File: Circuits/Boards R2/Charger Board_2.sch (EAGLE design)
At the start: 78 parts, among them CON1 ISP(2X3), CON10 HEADER_3X1, CON11 HEADER_3X1, CON12 HEADER_3X1, CON13 HEADER_4X1, CON2 SCREWTERMINAL_1X2, CON3 HEADER_3X1, CON4 HEADER_3X1, CON5 HEADER_3X1, CON6 HEADER_3X1, CON7 HEADER_3X1, CON8 HEADER_3X1, CON9 HEADER_3X1, IC1 NCP1117DT33G, T1 NPN2N2222, T2 NPN2N2222, T3 SI4421DY, U1 ATMEGA324P, U2 ACS711, U3 JOYSTICKPTH, U4 MX25L25735E

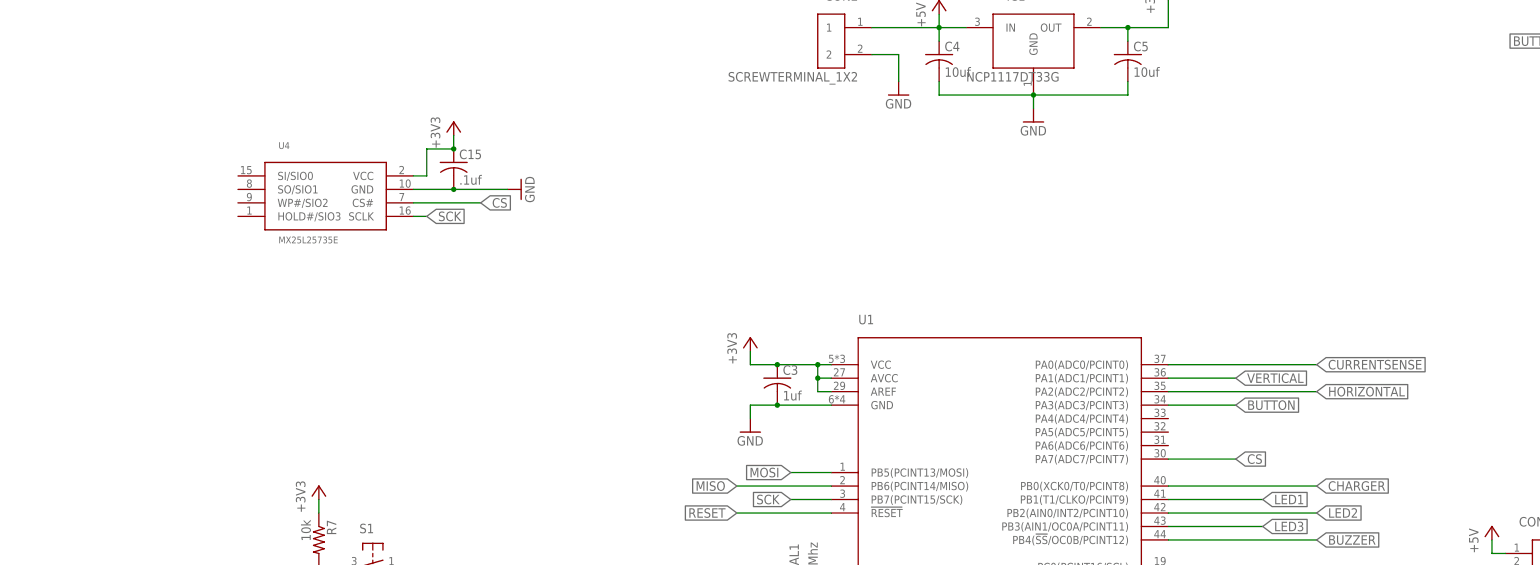
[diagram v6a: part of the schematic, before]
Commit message: completed schematic for the charger board
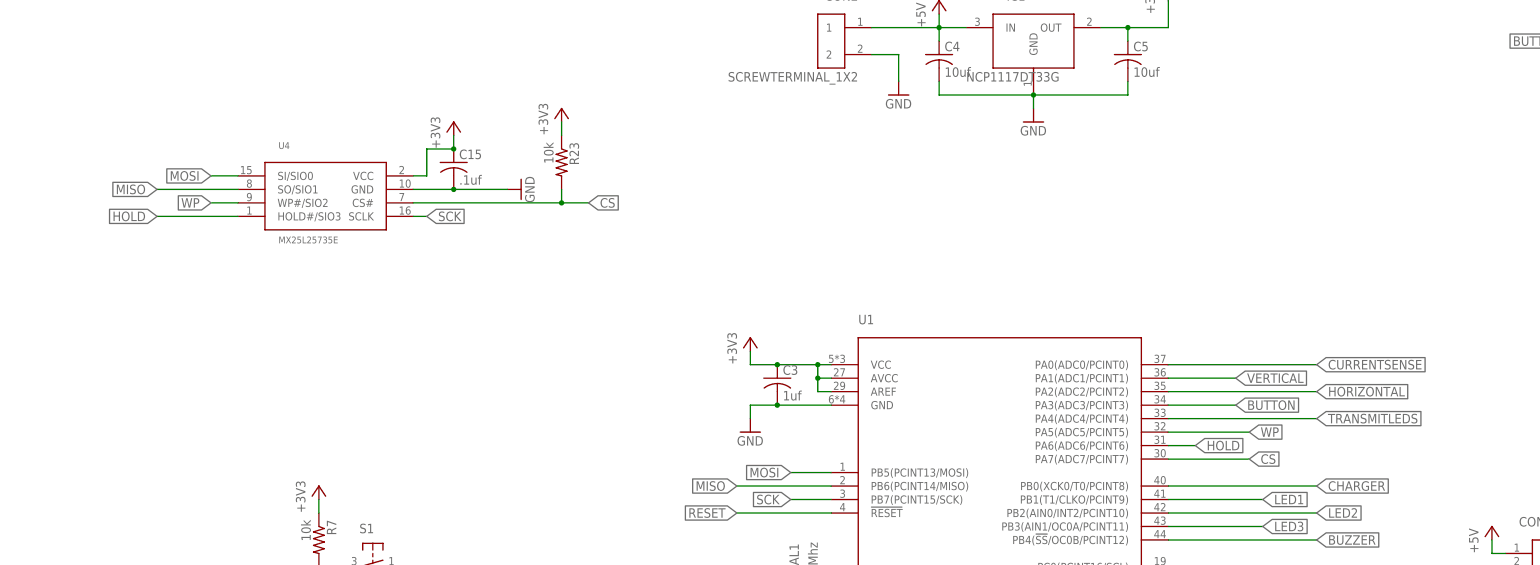
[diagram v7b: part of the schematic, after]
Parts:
- added R23: 10k, Passive:RES0603
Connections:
- new net HOLD: U1.PA6(ADC6/PCINT6), U4.HOLD#/SIO3
- new net WP: U1.PA5(ADC5/PCINT5), U4.WP#/SIO2
- net +3V3: now also R23.1
- net CS: now also R23.2
- net MISO: now also U4.SO/SIO1
- net MOSI: now also U4.SI/SIO0
- net TRANSMITLEDS: now also U1.PA4(ADC4/PCINT4)
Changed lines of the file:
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@@
 <part name="+3V1" library="Supply" deviceset="+3V3" device=""/>
 <part name="GND17" library="Supply" deviceset="GND" device=""/>
+<part name="R23" library="Passive" deviceset="RES" device="0603" value="10k"/>
+<part name="+3V11" library="Supply" deviceset="+3V3" device=""/>
 </parts>
 <sheets>
@@
 <instance part="+3V1" gate="G$1" x="-104.14" y="83.82"/>
 <instance part="GND17" gate="1" x="-91.44" y="71.12" rot="R90"/>
+<instance part="R23" gate="G$1" x="-83.82" y="76.2" rot="R270"/>
+<instance part="+3V11" gate="G$1" x="-83.82" y="86.36"/>
 </instances>
 <busses>
@@
 <wire x1="190.5" y1="43.18" x2="185.42" y2="43.18" width="0.1524" layer="91"/>
 <label x="185.42" y="43.18" size="1.778" layer="91" rot="R180" xref="yes"/>
+</segment>
+<segment>
+<pinref part="U1" gate="G$1" pin="PA4(ADC4/PCINT4)"/>
+<wire x1="30.48" y1="27.94" x2="58.42" y2="27.94" width="0.1524" layer="91"/>
+<label x="58.42" y="27.94" size="1.778" layer="91" xref="yes"/>
 </segment>
 </net>
@@
 <junction x="-104.14" y="78.74"/>
 </segment>
+<segment>
+<pinref part="R23" gate="G$1" pin="1"/>
+<wire x1="-83.82" y1="81.28" x2="-83.82" y2="83.82" width="0.1524" layer="91"/>
+<pinref part="+3V11" gate="G$1" pin="+3V3"/>
+</segment>
 </net>
 <net name="SECTION2" class="0">
@@
 <label x="-40.64" y="17.78" size="1.778" layer="91" rot="R180" xref="yes"/>
 </segment>
+<segment>
+<pinref part="U4" gate="G$1" pin="SI/SIO0"/>
+<wire x1="-144.78" y1="73.66" x2="-149.86" y2="73.66" width="0.1524" layer="91"/>
+<label x="-149.86" y="73.66" size="1.778" layer="91" rot="R180" xref="yes"/>
+</segment>
 </net>
 <net name="MISO" class="0">
@@
 <label x="-50.8" y="15.24" size="1.778" layer="91" rot="R180" xref="yes"/>
 </segment>
+<segment>
+<pinref part="U4" gate="G$1" pin="SO/SIO1"/>
+<wire x1="-144.78" y1="71.12" x2="-160.02" y2="71.12" width="0.1524" layer="91"/>
+<label x="-160.02" y="71.12" size="1.778" layer="91" rot="R180" xref="yes"/>
+</segment>
 </net>
 <net name="SCK" class="0">
@@
 <segment>
 <pinref part="U4" gate="G$1" pin="CS#"/>
-<wire x1="-111.76" y1="68.58" x2="-99.06" y2="68.58" width="0.1524" layer="91"/>
-<label x="-99.06" y="68.58" size="1.778" layer="91" xref="yes"/>
+<wire x1="-111.76" y1="68.58" x2="-83.82" y2="68.58" width="0.1524" layer="91"/>
+<label x="-78.74" y="68.58" size="1.778" layer="91" xref="yes"/>
+<pinref part="R23" gate="G$1" pin="2"/>
+<wire x1="-83.82" y1="68.58" x2="-78.74" y2="68.58" width="0.1524" layer="91"/>
+<wire x1="-83.82" y1="71.12" x2="-83.82" y2="68.58" width="0.1524" layer="91"/>
+<junction x="-83.82" y="68.58"/>
 </segment>
 <segment>
 <pinref part="U1" gate="G$1" pin="PA7(ADC7/PCINT7)"/>
-<wire x1="30.48" y1="20.32" x2="43.18" y2="20.32" width="0.1524" layer="91"/>
-<label x="43.18" y="20.32" size="1.778" layer="91" xref="yes"/>
-</segment>
-</net>
+<wire x1="30.48" y1="20.32" x2="45.72" y2="20.32" width="0.1524" layer="91"/>
+<label x="45.72" y="20.32" size="1.778" layer="91" xref="yes"/>
+</segment>
+</net>
+<net name="WP" class="0">
+<segment>
+<pinref part="U4" gate="G$1" pin="WP#/SIO2"/>
+<wire x1="-144.78" y1="68.58" x2="-149.86" y2="68.58" width="0.1524" layer="91"/>
+<label x="-149.86" y="68.58" size="1.778" layer="91" rot="R180" xref="yes"/>
+</segment>
+<segment>
+<pinref part="U1" gate="G$1" pin="PA5(ADC5/PCINT5)"/>
+<wire x1="30.48" y1="25.4" x2="45.72" y2="25.4" width="0.1524" layer="91"/>
+<label x="45.72" y="25.4" size="1.778" layer="91" xref="yes"/>
+</segment>
+</net>
+<net name="HOLD" class="0">
+<segment>
+<pinref part="U4" gate="G$1" pin="HOLD#/SIO3"/>
+<wire x1="-144.78" y1="66.04" x2="-160.02" y2="66.04" width="0.1524" layer="91"/>
+<label x="-160.02" y="66.04" size="1.778" layer="91" rot="R180" xref="yes"/>
+</segment>
+<segment>
+<pinref part="U1" gate="G$1" pin="PA6(ADC6/PCINT6)"/>
+<wire x1="30.48" y1="22.86" x2="35.56" y2="22.86" width="0.1524" layer="91"/>
+<label x="35.56" y="22.86" size="1.778" layer="91" xref="yes"/>
+</segment>
+</net>

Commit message: more board updates
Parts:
- added R24: 10k, Passive:RES0603
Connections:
- net +5V: now also R24.2
- net CHARGER: now also R24.1
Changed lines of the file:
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@@
 <part name="R23" library="Passive" deviceset="RES" device="0603" value="10k"/>
 <part name="+3V11" library="Supply" deviceset="+3V3" device=""/>
+<part name="R24" library="Passive" deviceset="RES" device="0603" value="10k"/>
+<part name="P+5" library="Supply" deviceset="+5V" device=""/>
 </parts>
 <sheets>
@@
 <instance part="R23" gate="G$1" x="-83.82" y="76.2" rot="R270"/>
 <instance part="+3V11" gate="G$1" x="-83.82" y="86.36"/>
+<instance part="R24" gate="G$1" x="-71.12" y="-68.58" rot="R90"/>
+<instance part="P+5" gate="1" x="-71.12" y="-58.42"/>
 </instances>
 <busses>
@@
 <pinref part="P+3" gate="1" pin="+5V"/>
 </segment>
+<segment>
+<pinref part="R24" gate="G$1" pin="2"/>
+<wire x1="-71.12" y1="-63.5" x2="-71.12" y2="-60.96" width="0.1524" layer="91"/>
+<pinref part="P+5" gate="1" pin="+5V"/>
+</segment>
 </net>
 <net name="CURRENTSENSE" class="0">
@@
 <net name="CHARGER" class="0">
 <segment>
-<wire x1="-63.5" y1="-76.2" x2="-76.2" y2="-76.2" width="0.1524" layer="91"/>
+<wire x1="-63.5" y1="-76.2" x2="-71.12" y2="-76.2" width="0.1524" layer="91"/>
 <label x="-76.2" y="-76.2" size="1.778" layer="91" rot="R180" xref="yes"/>
 <pinref part="T3" gate="G$1" pin="G"/>
-</segment>
-<segment>
+<pinref part="R24" gate="G$1" pin="1"/>
+<wire x1="-71.12" y1="-76.2" x2="-76.2" y2="-76.2" width="0.1524" layer="91"/>
+<wire x1="-71.12" y1="-73.66" x2="-71.12" y2="-76.2" width="0.1524" layer="91"/>
+<junction x="-71.12" y="-76.2"/>
+</segment>
+<segment>
